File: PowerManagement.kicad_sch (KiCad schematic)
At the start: 0 parts

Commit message: adding USB-C port for charging and data transfer
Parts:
- added J2: USB_C_Receptacle_USB2.0_16P, symbol Connector:USB_C_Receptacle_USB2.0_16P
- added R1: 5.1Ko, symbol Device:R
- added R2: 5.1 Ko, symbol Device:R
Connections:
- new net: J2.A5 (CC1), R1.1
- new net: J2.B5 (CC2), R2.1
- new net +5V: J2.A4 (VBUS), J2.A9 (VBUS), J2.B4 (VBUS), J2.B9 (VBUS)
- new net GND: J2.A1 (GND), J2.A12 (GND), J2.B1 (GND), J2.B12 (GND), J2.SH (SHIELD), R1.2, R2.2
- new net USB Data +: J2.A6 (D+), J2.B6 (D+)
- new net USB Data -: J2.A7 (D-), J2.B7 (D-)

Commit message: fixing uncommited errors
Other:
- note added: "USB-C Charging port"
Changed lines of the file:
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@@
 	(generator_version "10.0")
 	(paper "A4")
+	(rectangle
+		(start 12.7 12.7)
+		(end 86.36 87.63)
+		(stroke
+			(width 0)
+			(type default)
+		)
+		(fill
+			(type none)
+		)
+	)
+	(text "USB-C Charging port"
+		(exclude_from_sim no)
+		(at 74.93 86.106 0)
+		(effects
+			(font
+				(size 1.27 1.27)
+			)
+		)
+	)
 	(junction
 		(at 44.45 71.12)

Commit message: fixing project files
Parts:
- added C1: 4.7uF-47uF, symbol Device:C_Small
- added C2: 5uF, symbol Device:C_Small
- added D1: LED, symbol Device:LED
- added J1: Conn_01x03_Pin, symbol Connector:Conn_01x03_Pin
- added R3, R4: 1.0Ko, symbol Device:R
- added U1: BQ24074RGT, Package_DFN_QFN:VQFN-16-1EP_3x3mm_P0.5mm_EP1.6x1.6mm, symbol Battery_Management:BQ24074RGT
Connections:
- net +5V: now also U1.13 (IN), U1.5 (EN2)
- net GND: now also R3.1, U1.6 (EN1)
- new net: C1.1, C2.1, D1.1 (K), R4.1
- new net: C2.2, U1.17 (VSS), U1.8 (VSS)
- new net: R3.2, U1.12 (ILIM)
- new net: J1.3 (Pin_3), U1.10 (OUT), U1.11 (OUT)
- new net: R4.2, U1.16 (ISET)
- new net: U1.2 (BAT), U1.3 (BAT)
- new net: D1.2 (A), U1.9 (~{CHG})
- new net: C1.2, J1.1 (Pin_1)

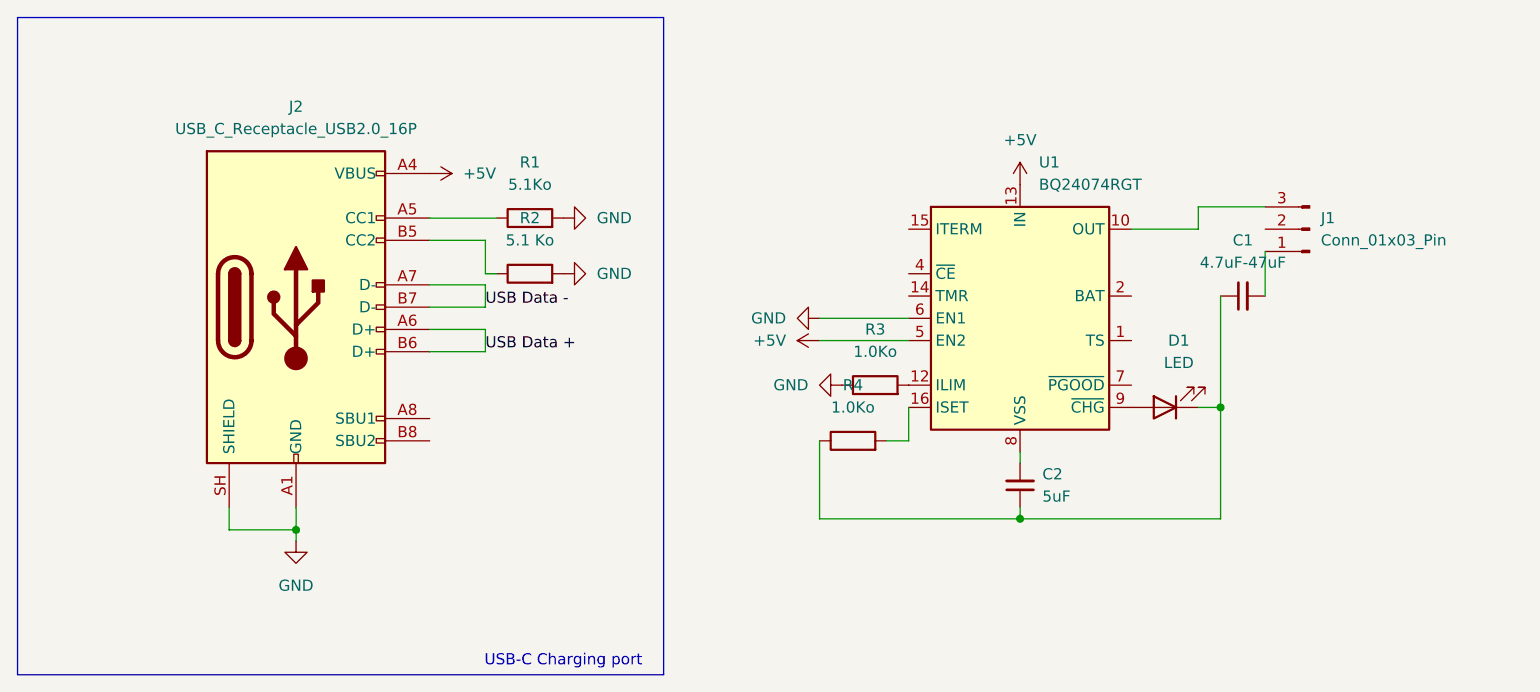
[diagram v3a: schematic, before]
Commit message: getting the bq24074rtg wired properly
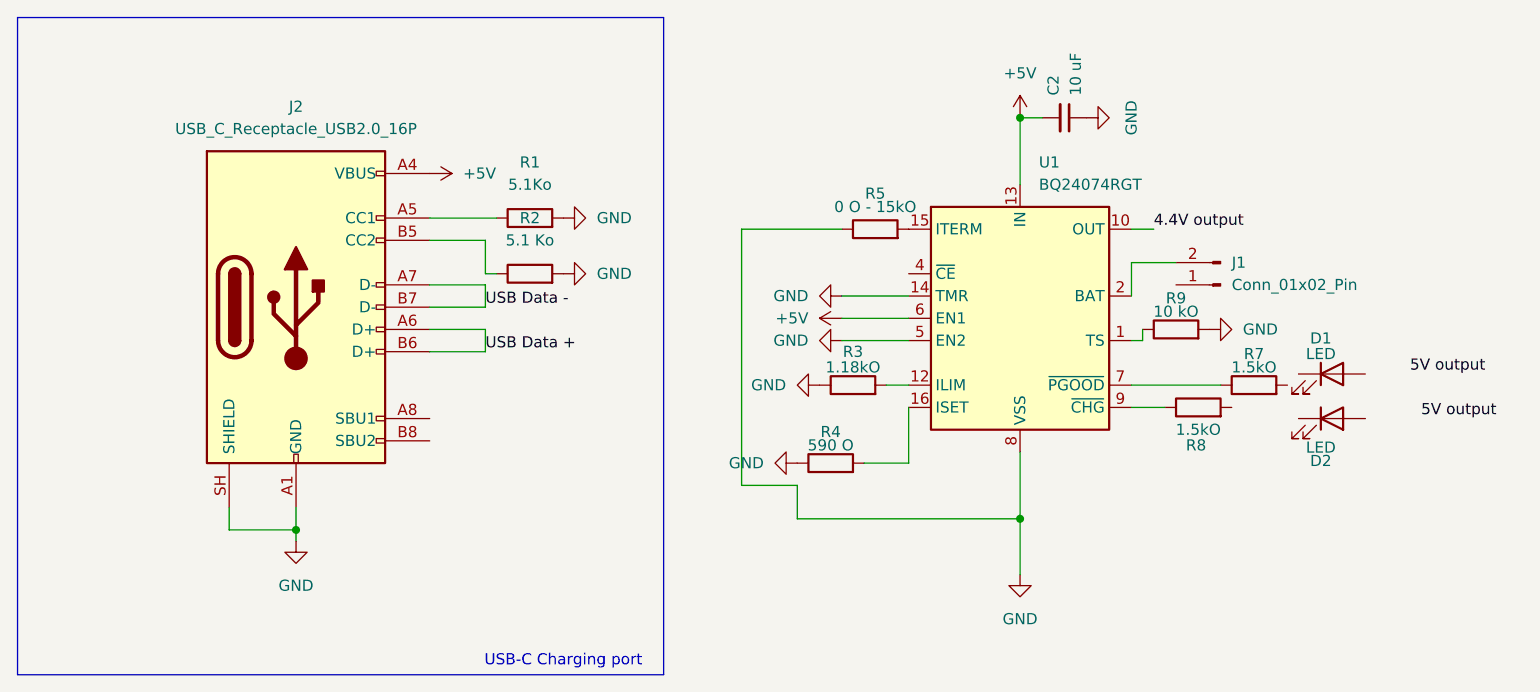
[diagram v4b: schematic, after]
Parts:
- removed C1: 4.7uF-47uF, symbol Device:C_Small
- removed J1: Conn_01x03_Pin, symbol Connector:Conn_01x03_Pin
- added D2: LED, symbol Device:LED
- added J1: Conn_01x02_Pin, symbol Connector:Conn_01x02_Pin
- added R5: 0 O - 15kO, symbol Device:R
- added R7, R8: 1.5kO, symbol Device:R
- added R9: 10 kO, symbol Device:R
- C2: value 5uF -> 10 uF
- R3: value 1.0Ko -> 1.18kO
- R4: value 1.0Ko -> 590 O; footprint (none) -> scotto:Resistor_0402
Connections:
- net +5V: now also C2.2, U1.6 (EN1); no longer U1.5 (EN2)
- net GND: now also C2.1, R4.1, U1.14 (TMR), U1.17 (VSS), U1.5 (EN2), U1.8 (VSS), R5.1, R9.2; no longer U1.6 (EN1)
- net at U1.1 (TS): now also R9.1
- net 4.4V output: now reaches U1.10 (OUT), U1.11 (OUT)
- net at U1.15 (ITERM): now also R5.2
- net at U1.2 (BAT), U1.3 (BAT): now also J1.2 (Pin_2)
- net at U1.7 (~{PGOOD}): now also R7.1
- net at D1.2 (A): no longer U1.9 (~{CHG})
- new net: R8.1, U1.9 (~{CHG})
- now unconnected: D1.1 (K)
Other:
- moved on the sheet: C2, R3, R4
